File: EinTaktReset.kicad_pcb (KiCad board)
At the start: 2 copper layers, 100 x 160 mm, 59 parts, among them IC1 74LS624, J1 3PinTerminalBlocktg, J2 3PinTerminalBlocktg, J3 2PinTerminalBlocktg, J4 3PinTerminalBlocktg, J5 2PinTerminalBlocktg, P1 CONN_02X10, P4 CONN_02X10, SW1 SWITCH_INV, SW10 SPST, SW11 SPST, SW12 SPST, SW13 SPST, SW2 SWITCH_INV, SW3 SPST, SW4 SPST, SW5 SPST, SW6 SWITCH_INV, SW7 SPST, SW8 SPST, SW9 SPST, U1 74LS132, U2 74540En, U3 74HCT541_PWR, U4 74LS32, U5 74LS00

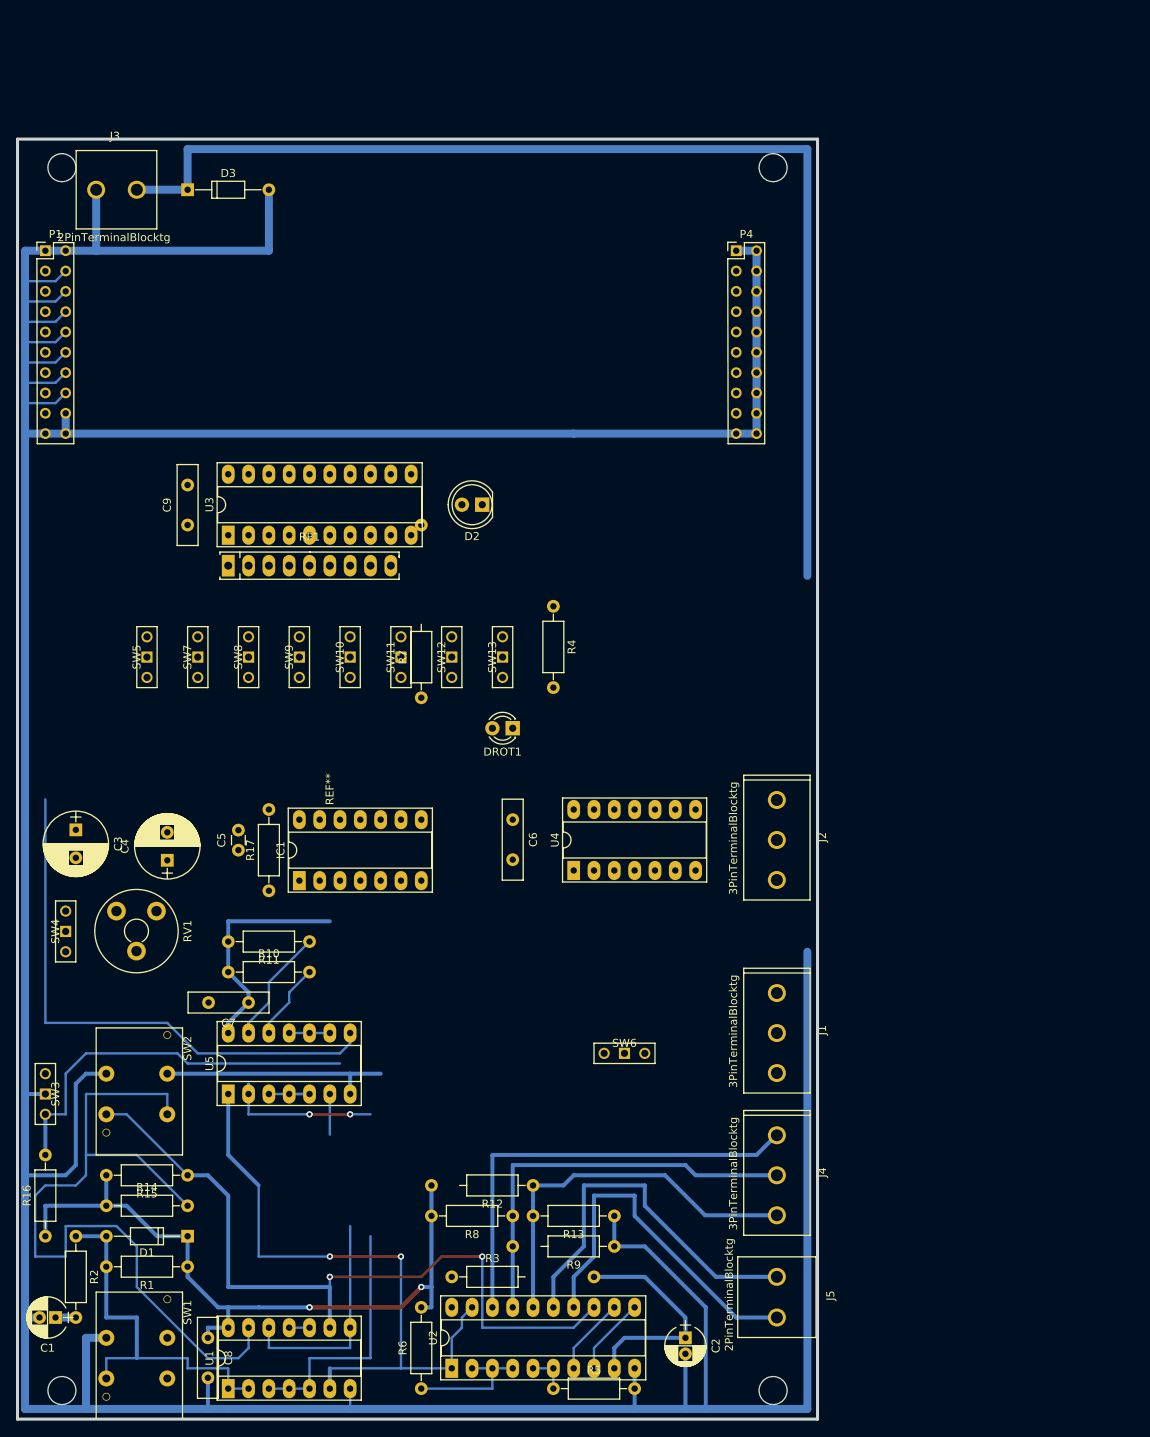
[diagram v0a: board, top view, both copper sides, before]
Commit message: EinTaktReset: Fehler in .sch behoben (Details in todo), Verbindungen großteils gelegt, todo updated
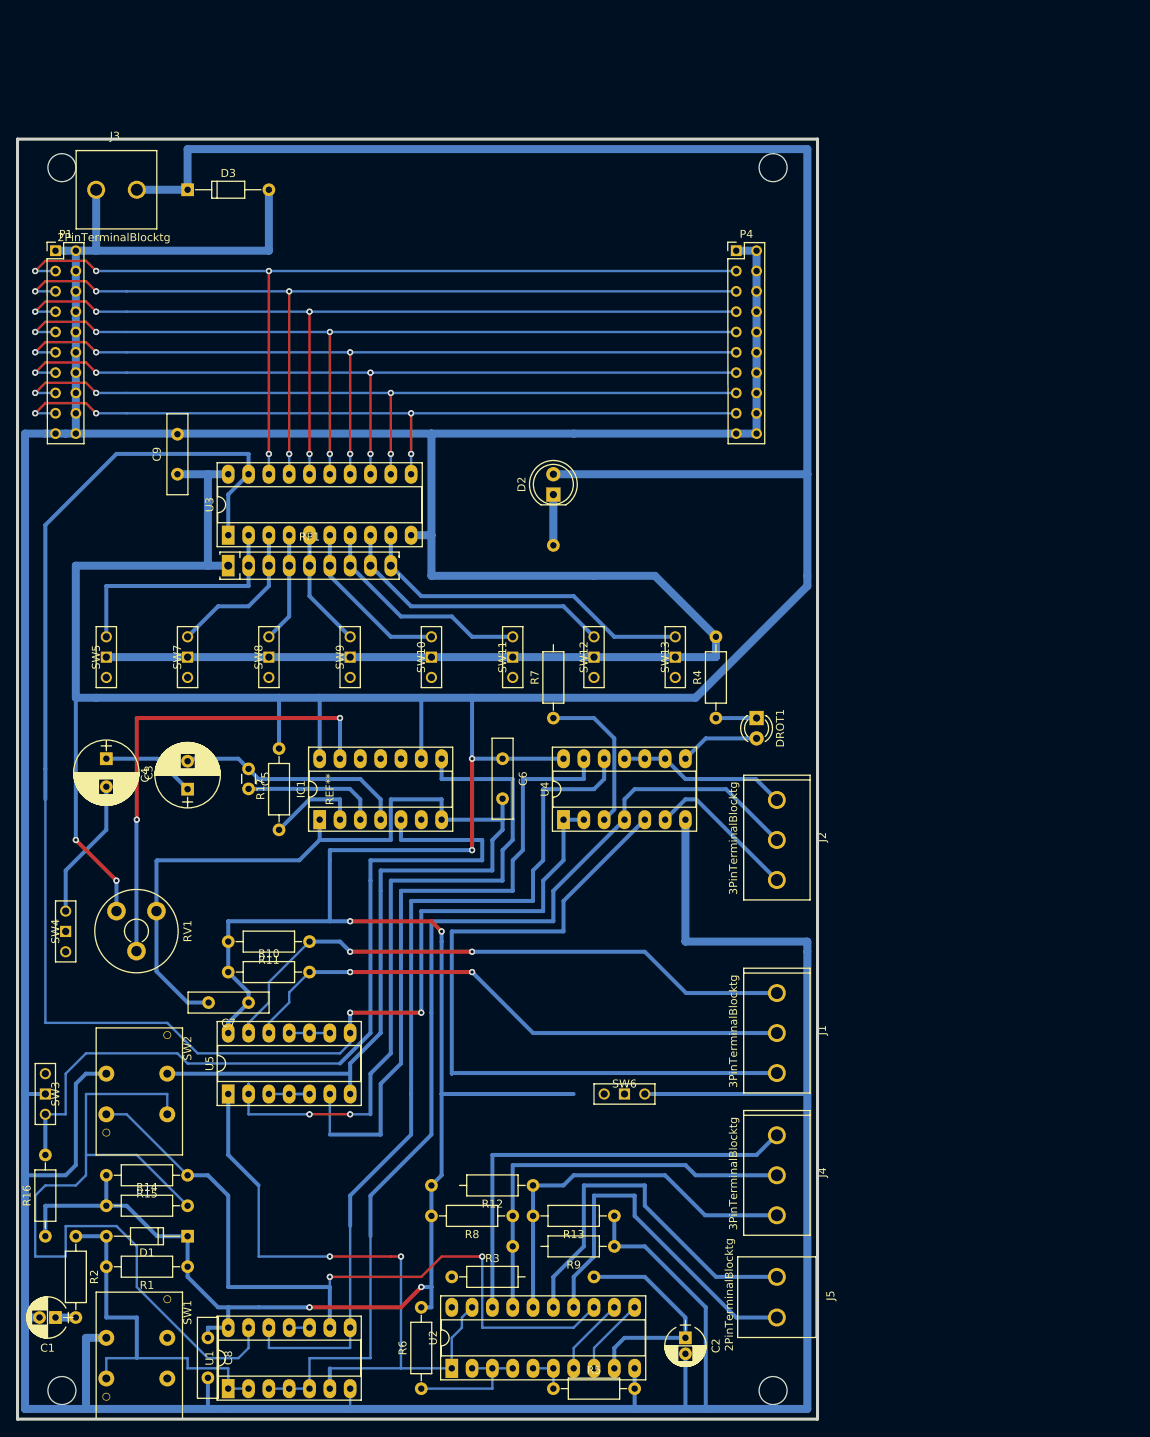
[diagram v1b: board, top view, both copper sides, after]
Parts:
- moved DROT1 30.5 mm to (101.6, 113.0), turned to 270 degrees
- moved R4 24.7 mm to (96.5, 113.0), turned to 90 degrees
- moved SW13 21.6 mm to (91.4, 108.0)
- moved SW12 17.8 mm to (81.3, 108.0)
- moved R7 16.7 mm to (76.2, 113.0)
- moved SW11 14.0 mm to (71.1, 108.0)
- moved C5 10.2 mm to (38.1, 119.4), turned to 270 degrees
- moved SW10 10.2 mm to (61.0, 108.0)
- moved C3 9.67 mm to (20.3, 118.1)
- moved C4 9.25 mm to (30.5, 121.9)
- moved D2 8.98 mm to (76.2, 85.1), turned to 90 degrees
- moved IC1 8.03 mm to (47.0, 125.7)
- moved C6 7.73 mm to (69.8, 118.1)
- moved R17 7.73 mm to (41.9, 127.0)
- moved C9 6.48 mm to (29.2, 82.5)
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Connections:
- DROT1 pad 1: GND -> Net-(DROT1-Pad1)
- IC1 pad 7: Net-(IC1-Pad7) -> GND
- IC1 pad 9: Net-(IC1-Pad9) -> VCC
- R4 pad 1: Net-(R4-Pad1) -> Net-(DROT1-Pad1)
- R4 pad 2: Net-(DROT1-Pad2) -> GND
- U4 pad 2: Net-(U4-Pad2) -> Net-(U3-Pad1)
- U4 pad 8: Net-(R4-Pad1) -> Net-(DROT1-Pad2)
- U5 pad 8: Net-(U4-Pad2) -> Net-(U3-Pad1)
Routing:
- net VCC: track 259.0 -> 613.4 mm, vias 2 -> 8
- net GND: track 619.9 -> 887.2 mm
- net Net-(U3-Pad1): track 0.00 -> 198.4 mm, vias 0 -> 2
- net /a0: track 0.00 -> 116.6 mm, vias 0 -> 4
- net /a1: track 0.00 -> 114.1 mm, vias 0 -> 4
- net /a2: track 0.00 -> 111.5 mm, vias 0 -> 4
- net /a3: track 0.00 -> 109.0 mm, vias 0 -> 4
- net /a4: track 0.00 -> 106.5 mm, vias 0 -> 4
- net /a5: track 0.00 -> 103.9 mm, vias 0 -> 4
- net /a6: track 0.00 -> 101.4 mm, vias 0 -> 4
- net enDEC: track 31.7 -> 130.6 mm
- net /a7: track 0.00 -> 98.8 mm, vias 0 -> 4
- net auto: track 0.00 -> 90.6 mm
- net Net-(U1-Pad12): track 27.9 -> 112.2 mm
- net Net-(U4-Pad13): track 5.08 -> 81.6 mm
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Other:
- net class Default: trace_width 1 -> 0.5

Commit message: EinTaktReset: Fehler behoben (Details in todo), PCB jetzt Fehlerfrei
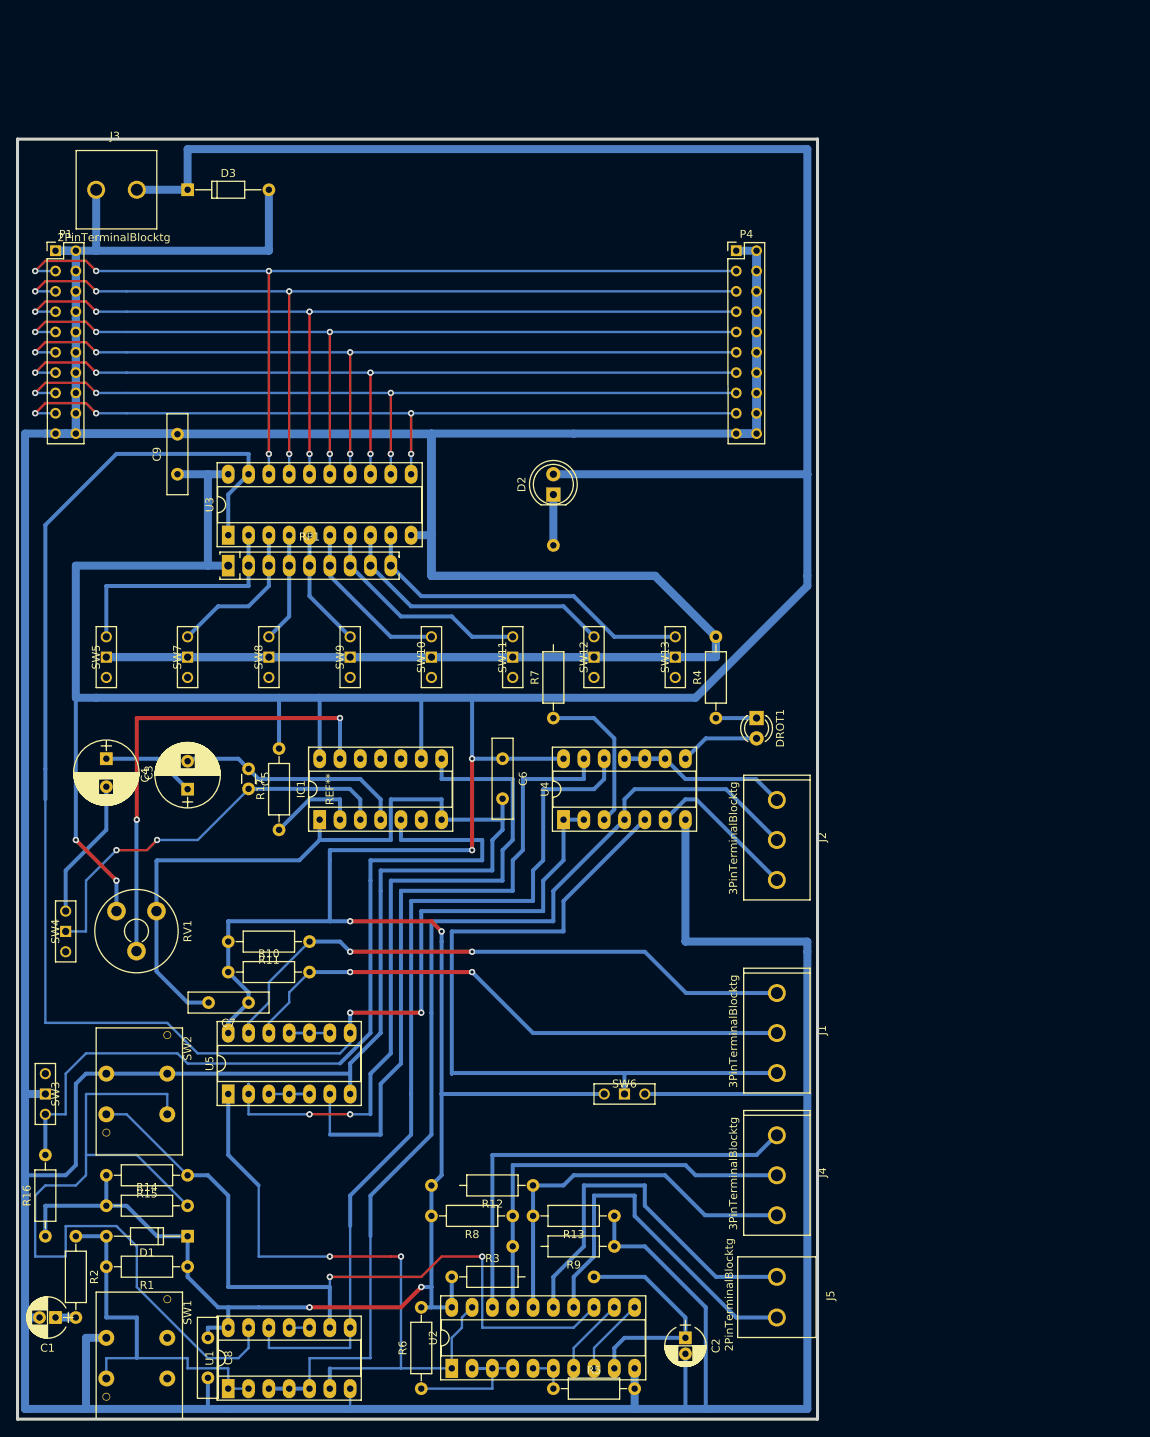
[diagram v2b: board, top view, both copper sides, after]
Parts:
- removed the REF** at (109.2, 200.7)
- added REF**: EuroBoard160mmX100mm, EuroBoard_Outline:EuroBoard160mmX100mm, F.Cu at (109.2, 200.7)
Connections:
- SW6 pad 0: auto -> VCC
- SW6 pad 1: VCC -> auto
- U2 pad 20: (no net) -> VCC
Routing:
- net GND: track 887.2 -> 1199.0 mm
- net Net-(C5-Pad2): track 17.1 -> 51.0 mm, vias 0 -> 2
- net VCC: track 613.4 -> 623.6 mm
- net CLK: track 21.2 -> 26.3 mm
- net enDEC: track 130.6 -> 135.7 mm
- net auto: track 90.6 -> 93.4 mm
- net Net-(U5-Pad10): track 5.08 -> 7.62 mm
- net Net-(R6-Pad1): track 16.5 -> 19.0 mm

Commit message: track width geändert
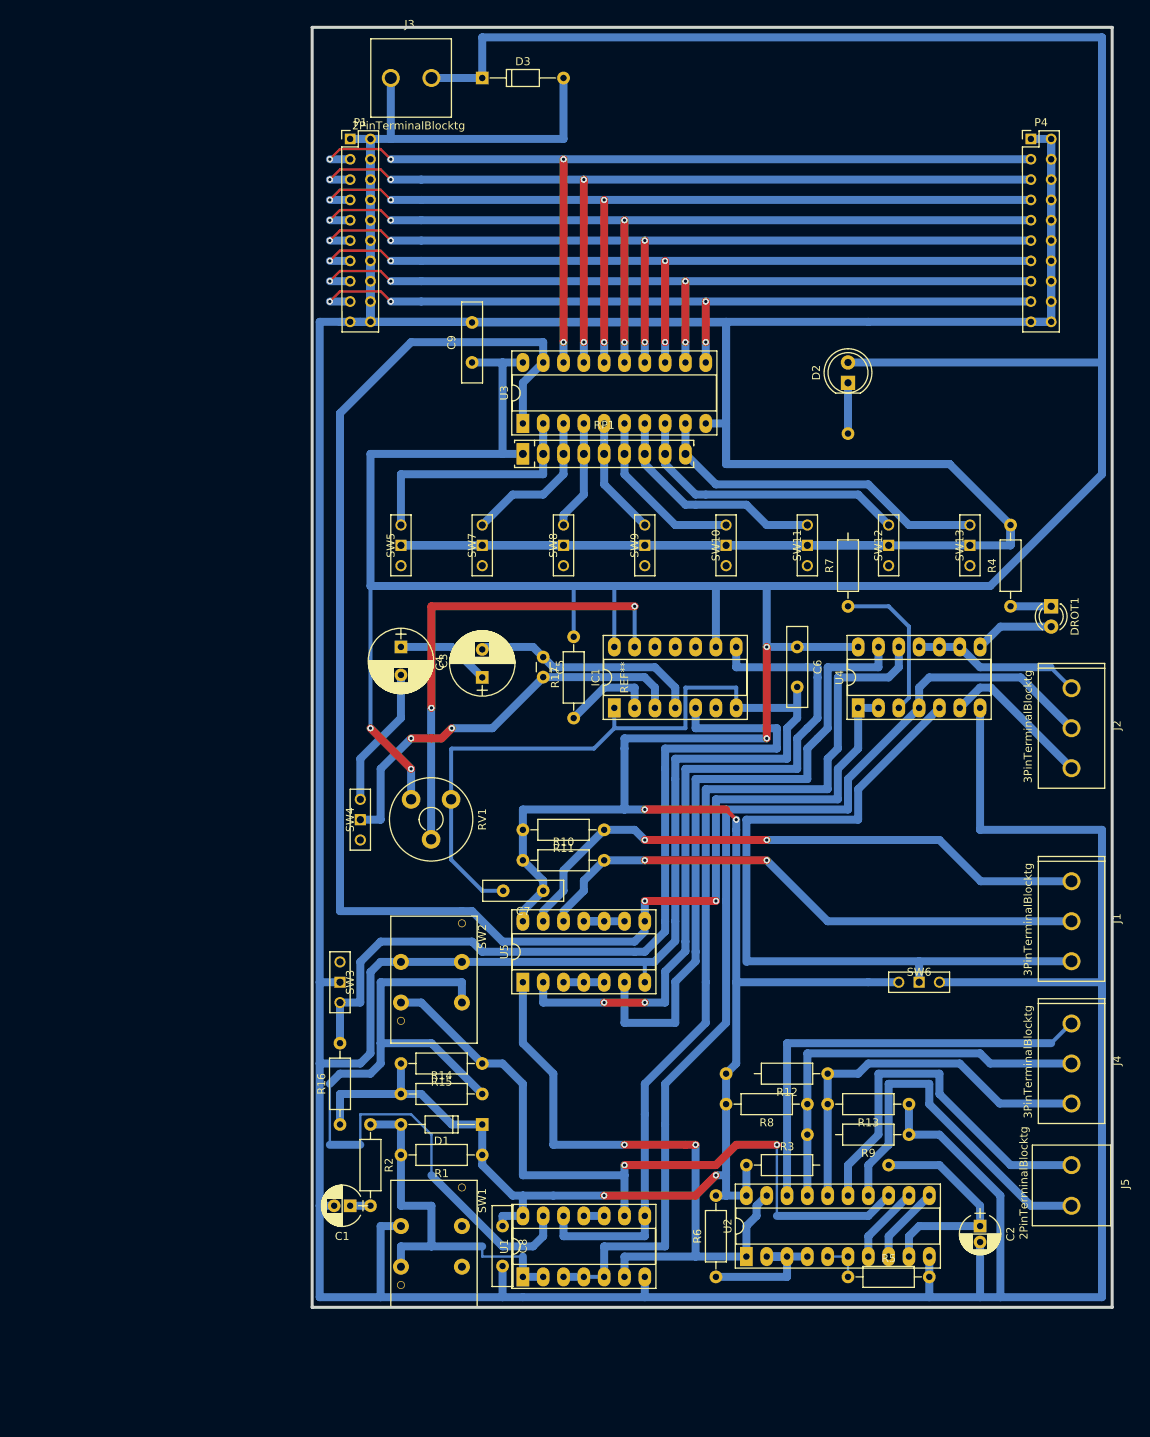
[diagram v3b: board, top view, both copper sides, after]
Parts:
- moved C5 39.4 mm to (74.9, 105.4)
- moved C6 39.4 mm to (106.7, 104.1)
- moved C7 39.4 mm to (74.9, 134.6)
- moved C9 39.4 mm to (66.0, 68.6)
- moved DROT1 39.4 mm to (138.4, 99.1)
- moved R1 39.4 mm to (67.3, 167.6)
- moved R13 39.4 mm to (120.7, 161.3)
- moved R9 39.4 mm to (120.7, 165.1)
- moved REF** 39.4 mm to (146.1, 186.7)
- moved SW10 39.4 mm to (97.8, 94.0)
- moved SW13 39.4 mm to (128.3, 94.0)
- moved C1 39.4 mm to (50.8, 174.0)
- moved C2 39.4 mm to (129.5, 176.5)
- moved C3 39.4 mm to (57.1, 104.1)
- moved C4 39.4 mm to (67.3, 108.0)
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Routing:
- net GND: track 1199.0 -> 1112.7 mm
- net CLK: track 26.3 -> 21.2 mm
- net Net-(IC1-Pad8): track 89.2 -> 88.5 mm
- net Net-(U4-Pad13): track 81.6 -> 80.8 mm
- net Net-(RP1-Pad7): track 27.8 -> 28.6 mm
- net Net-(RP1-Pad6): track 20.9 -> 21.7 mm
- net Net-(RP1-Pad8): track 35.4 -> 36.2 mm
- net Net-(IC1-Pad5): track 104.8 -> 105.5 mm
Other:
- net class Default: trace_width 0.5 -> 1

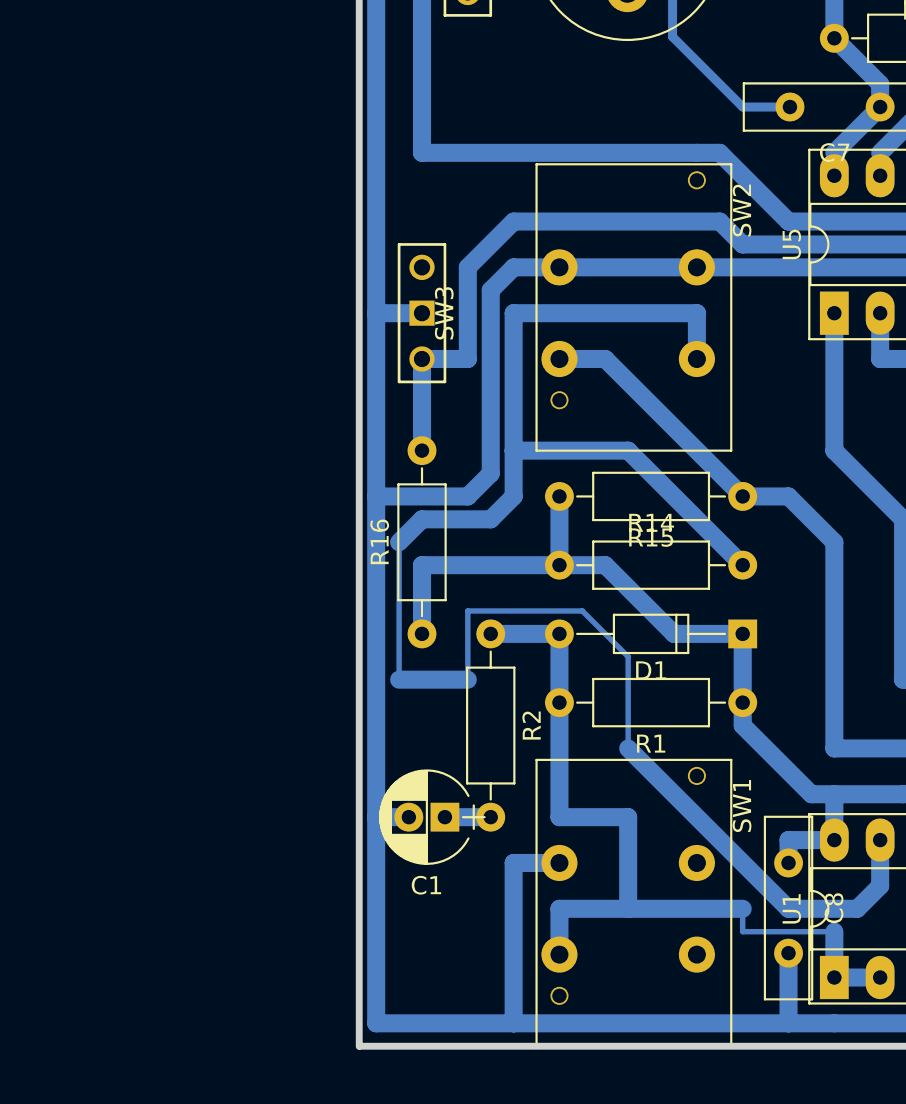
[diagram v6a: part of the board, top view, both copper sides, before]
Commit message: Eintakt libs fixed
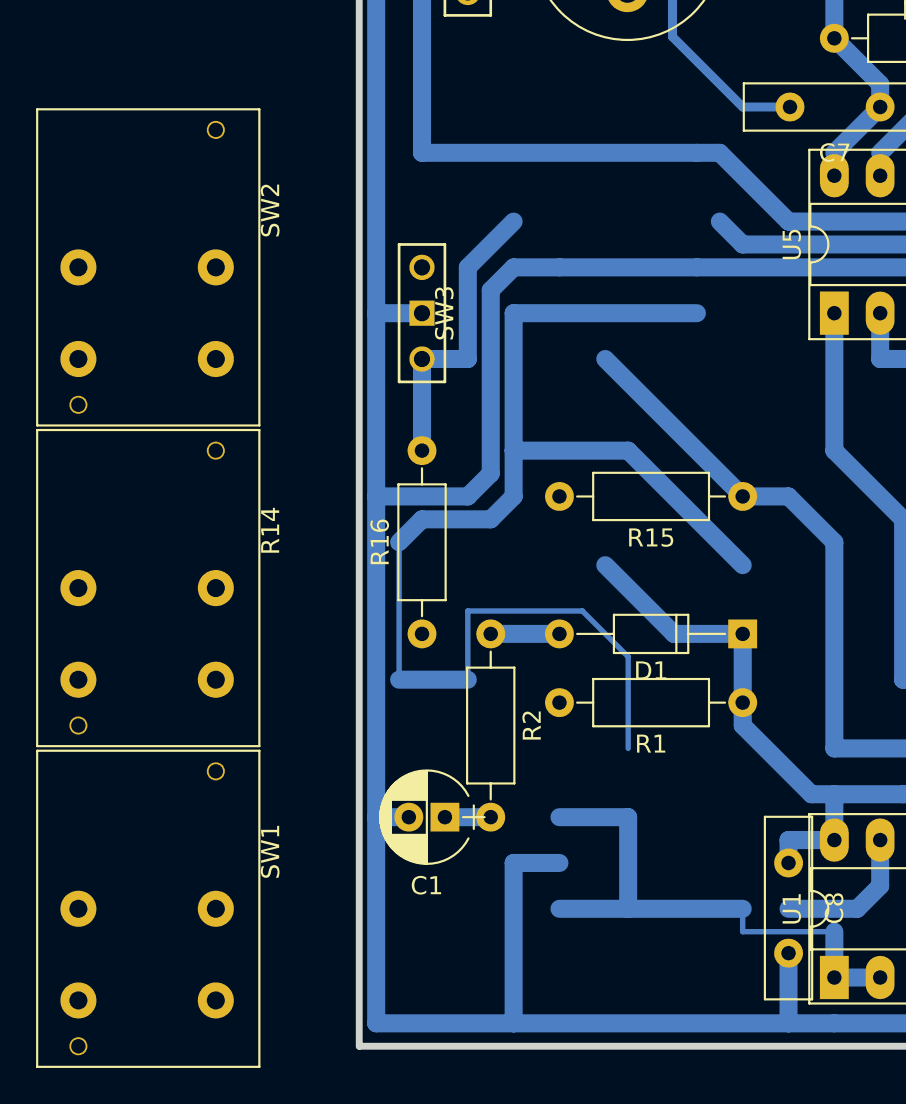
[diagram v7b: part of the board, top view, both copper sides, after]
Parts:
- R14: footprint Resistors_ThroughHole:R_Axial_DIN0207_L6.3mm_D2.5mm_P10.16mm_Horizontal -> tg_foodprint:SW_PUSH_LCD_E3_SAxxxx_tg_V2
- SW1, SW2: footprint tg_foodprint:SW_PUSH_LCD_E3_SAxxxx_tg -> tg_foodprint:SW_PUSH_LCD_E3_SAxxxx_tg_V2
- moved SW2 27.1 mm to (38.1, 143.5)
- moved SW1 26.8 mm to (38.1, 179.1)
- moved R14 19.1 mm to (38.1, 161.3), turned to 270 degrees
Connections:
- IC1 pad 6: Net-(IC1-Pad6) -> (no net)
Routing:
- net VCC: track 623.6 -> 605.8 mm
- net Net-(R14-Pad2): track 96.6 -> 81.5 mm
- net Net-(D1-Pad2): track 47.0 -> 34.3 mm
- net Net-(IC1-Pad5): track 105.5 -> 94.1 mm
- net Net-(R15-Pad1): track 93.9 -> 91.4 mm
